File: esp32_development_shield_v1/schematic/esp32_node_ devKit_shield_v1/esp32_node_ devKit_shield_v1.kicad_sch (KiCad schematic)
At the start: 37 parts, among them J1 Screw_Terminal_01x02, J10 Screw_Terminal_01x02, J11 Screw_Terminal_01x02, J12 Screw_Terminal_01x02, J13 Screw_Terminal_01x02, J14 Screw_Terminal_01x02, J15 Screw_Terminal_01x02, J16 Screw_Terminal_01x02, J17 Screw_Terminal_01x02, J19 Screw_Terminal_01x02, J2 Conn_02x20_Odd_Even, J20 Screw_Terminal_01x02, J21 Screw_Terminal_01x02, J22 Screw_Terminal_01x02, J23 Screw_Terminal_01x02, J24 Screw_Terminal_01x02, J25 Screw_Terminal_01x02, J26 Screw_Terminal_01x02, J27 Conn_01x04, J28 Conn_01x04, J29 Conn_01x04, J3 Conn_02x20_Odd_Even, J30 Conn_01x04, J31 USB_C_Receptacle_PowerOnly_6P, J4 Conn_01x04, J5 Conn_01x04, J6 Conn_01x04, J7 Conn_01x04, J8 Screw_Terminal_01x02, J9 Screw_Terminal_01x02, U2 AMS1117-3.3

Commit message: *
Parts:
- removed J2, J3: Conn_02x20_Odd_Even, Connector_PinSocket_2.54mm:PinSocket_2x20_P2.54mm_Vertical, symbol Connector_Generic:Conn_02x20_Odd_Even
- added J18, J32: Conn_01x18_Pin, Connector_PinSocket_2.54mm:PinSocket_1x18_P2.54mm_Vertical, symbol Connector:Conn_01x18_Pin
- added J2, J3: Conn_02x19_Odd_Even, Connector_PinSocket_2.54mm:PinSocket_2x19_P2.54mm_Vertical, symbol Connector_Generic:Conn_02x19_Odd_Even
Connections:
- net 5V: now also J18.17 (Pin_17), J2.37 (Pin_37), J2.38 (Pin_38), J32.17 (Pin_17)
- net GND: now also J18.18 (Pin_18), J2.27 (Pin_27), J2.28 (Pin_28), J3.1 (Pin_1), J3.13 (Pin_13), J3.14 (Pin_14), J3.2 (Pin_2), J32.18 (Pin_18)
- net at J21.1 (Pin_1): now also J18.12 (Pin_12), J2.25 (Pin_25), J2.26 (Pin_26)
- net at J21.2 (Pin_2): now also J18.11 (Pin_11), J2.23 (Pin_23), J2.24 (Pin_24)
- net at J13.1 (Pin_1): now also J3.25 (Pin_25), J3.26 (Pin_26), J32.11 (Pin_11)
- net at J13.2 (Pin_2): now also J3.27 (Pin_27), J3.28 (Pin_28), J32.12 (Pin_12)
- net at J20.1 (Pin_1): now also J18.14 (Pin_14), J2.31 (Pin_31), J2.32 (Pin_32)
- net at J20.2 (Pin_2): now also J18.13 (Pin_13), J2.29 (Pin_29), J2.30 (Pin_30)
- net at J12.1 (Pin_1): now also J3.21 (Pin_21), J3.22 (Pin_22), J32.9 (Pin_9)
- net at J12.2 (Pin_2): now also J3.23 (Pin_23), J3.24 (Pin_24), J32.10 (Pin_10)
- net at J15.1 (Pin_1): now also J3.33 (Pin_33), J3.34 (Pin_34), J32.15 (Pin_15)
- net at J15.2 (Pin_2): now also J3.35 (Pin_35), J3.36 (Pin_36), J32.16 (Pin_16)
- net at J24.1 (Pin_1): now also J18.6 (Pin_6), J2.13 (Pin_13), J2.14 (Pin_14)
- net at J24.2 (Pin_2): now also J18.5 (Pin_5), J2.11 (Pin_11), J2.12 (Pin_12)
- net at J9.1 (Pin_1): now also J3.7 (Pin_7), J3.8 (Pin_8), J32.3 (Pin_3)
- net at J9.2 (Pin_2): now also J3.10 (Pin_10), J3.9 (Pin_9), J32.4 (Pin_4)
- net at J19.1 (Pin_1): now also J18.16 (Pin_16), J3.37 (Pin_37), J3.38 (Pin_38)
- net at J19.2 (Pin_2): now also J18.15 (Pin_15), J2.33 (Pin_33), J2.34 (Pin_34)
- net at J8.1 (Pin_1): now also J3.3 (Pin_3), J3.4 (Pin_4), J32.1 (Pin_1)
- net at J8.2 (Pin_2): now also J3.5 (Pin_5), J3.6 (Pin_6), J32.2 (Pin_2)
- net at J23.1 (Pin_1): now also J18.8 (Pin_8), J2.17 (Pin_17), J2.18 (Pin_18)
- net at J23.2 (Pin_2): now also J18.7 (Pin_7), J2.15 (Pin_15), J2.16 (Pin_16)
- net at J25.1 (Pin_1): now also J18.4 (Pin_4), J2.10 (Pin_10), J2.9 (Pin_9)
- net at J25.2 (Pin_2): now also J18.3 (Pin_3), J2.7 (Pin_7), J2.8 (Pin_8)
- net at J22.2 (Pin_2): now also J18.9 (Pin_9), J2.19 (Pin_19), J2.20 (Pin_20)
- net at J22.1 (Pin_1): now also J18.10 (Pin_10), J2.21 (Pin_21), J2.22 (Pin_22)
- net at J26.2 (Pin_2): now also J18.1 (Pin_1), J2.3 (Pin_3), J2.4 (Pin_4)
- net at J26.1 (Pin_1): now also J18.2 (Pin_2), J2.5 (Pin_5), J2.6 (Pin_6)
- net at J11.1 (Pin_1): now also J3.17 (Pin_17), J3.18 (Pin_18), J32.7 (Pin_7)
- net at J11.2 (Pin_2): now also J3.19 (Pin_19), J3.20 (Pin_20), J32.8 (Pin_8)
- net at J14.1 (Pin_1): now also J3.29 (Pin_29), J3.30 (Pin_30), J32.13 (Pin_13)
- net at J14.2 (Pin_2): now also J3.31 (Pin_31), J3.32 (Pin_32), J32.14 (Pin_14)
- net at J10.1 (Pin_1): now also J3.11 (Pin_11), J3.12 (Pin_12), J32.5 (Pin_5)
- net at J10.2 (Pin_2): now also J3.15 (Pin_15), J3.16 (Pin_16), J32.6 (Pin_6)
- no-connect marks 8 -> 4
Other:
- moved on the sheet: C1, C2, C3, J1, J10, J11, J12, J13, J14, J15, J16, J17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

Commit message: *
Replaced socket with header
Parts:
- J18, J32: footprint Connector_PinSocket_2.54mm:PinSocket_1x18_P2.54mm_Vertical -> Connector_PinHeader_2.54mm:PinHeader_1x18_P2.54mm_Vertical
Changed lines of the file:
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@@
 			)
 		)
-		(property "Footprint" "Connector_PinSocket_2.54mm:PinSocket_1x18_P2.54mm_Vertical"
+		(property "Footprint" "Connector_PinHeader_2.54mm:PinHeader_1x18_P2.54mm_Vertical"
 			(at 34.29 93.98 0)
 			(hide yes)
@@
 			)
 		)
-		(property "Footprint" "Connector_PinSocket_2.54mm:PinSocket_1x18_P2.54mm_Vertical"
+		(property "Footprint" "Connector_PinHeader_2.54mm:PinHeader_1x18_P2.54mm_Vertical"
 			(at 171.45 93.98 0)
 			(hide yes)

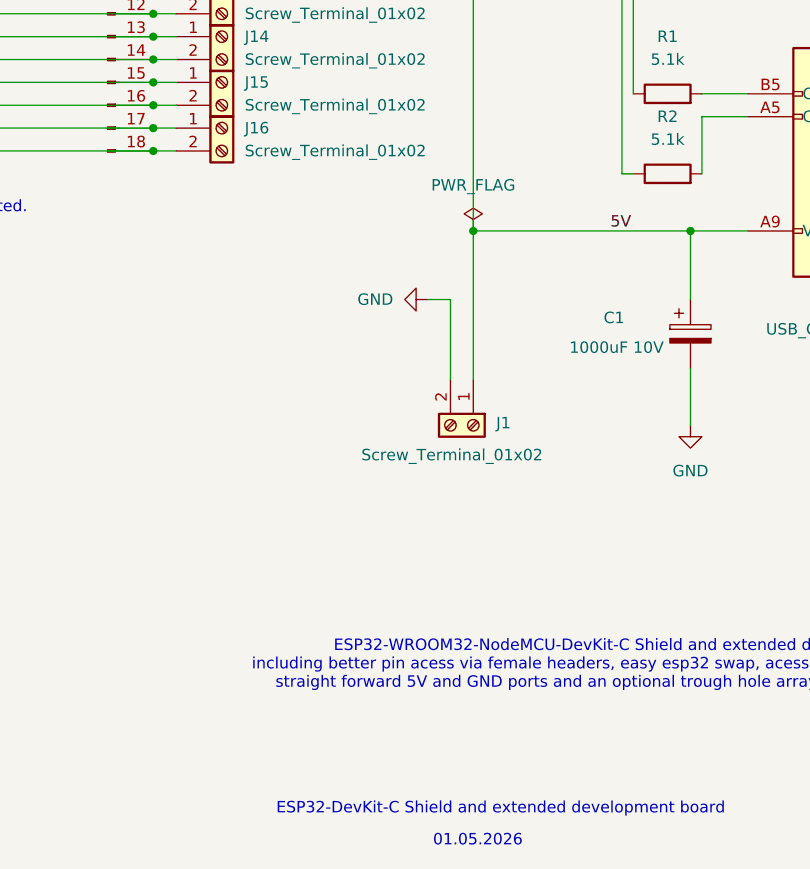
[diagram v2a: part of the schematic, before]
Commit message: Added LED for power on/off
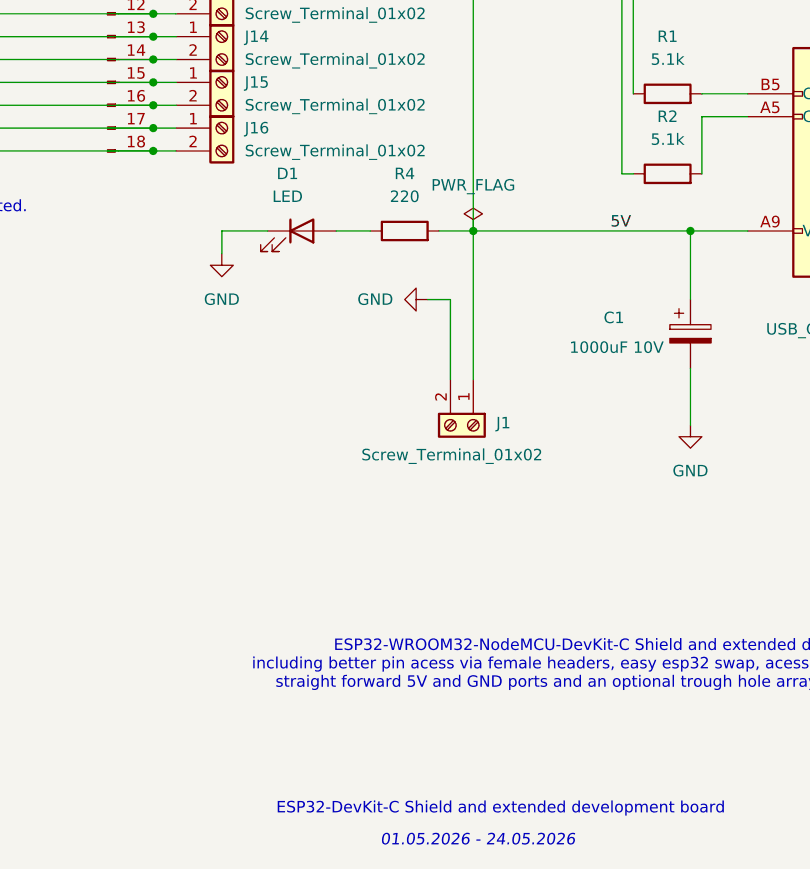
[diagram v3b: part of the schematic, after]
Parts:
- added D1: LED, LED_THT:LED_Rectangular_W3.0mm_H2.0mm, symbol Device:LED
- added R4: 220, Resistor_THT:R_Axial_DIN0207_L6.3mm_D2.5mm_P10.16mm_Horizontal, symbol Device:R
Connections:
- net 5V: now also R4.2
- net GND: now also D1.1 (K)
- new net: D1.2 (A), R4.1
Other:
- note added: "01.05.2026 - 24.05.2026"
- note removed: "01.05.2026"
